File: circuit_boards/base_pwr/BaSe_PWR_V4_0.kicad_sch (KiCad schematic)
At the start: 105 parts, among them J1 12VDC In, J1 USB_C_Receptacle, J10 Conn_01x04_Socket, J11 MOTOR, J3 USB3_A, J3 USB_B_Micro, J4 Conn_01x07_Pin, J5 Conn_02x06_Odd_Even, J7 Conn_02x06_Odd_Even, J7 USB3_B_Micro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

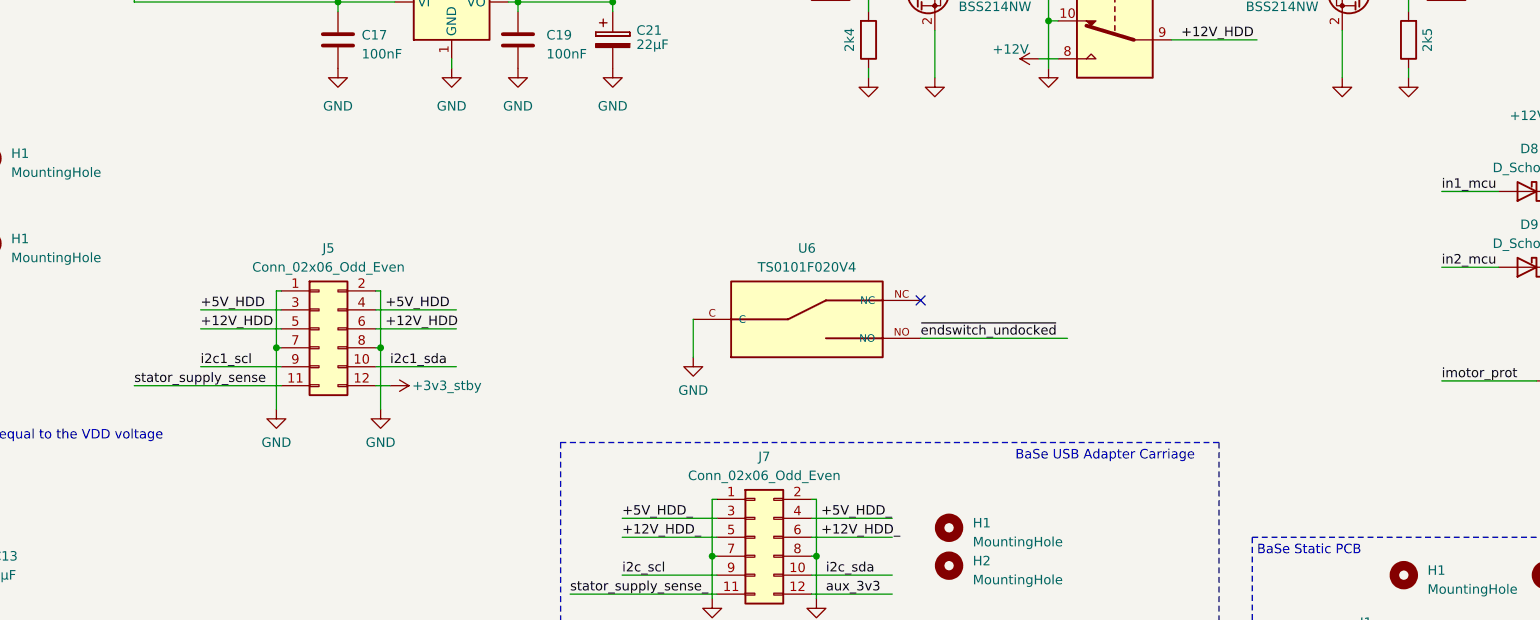
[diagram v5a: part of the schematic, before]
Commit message: BaSe PWR V4.0: rotate b2b connectors 180 degree for shorter pwr tracks
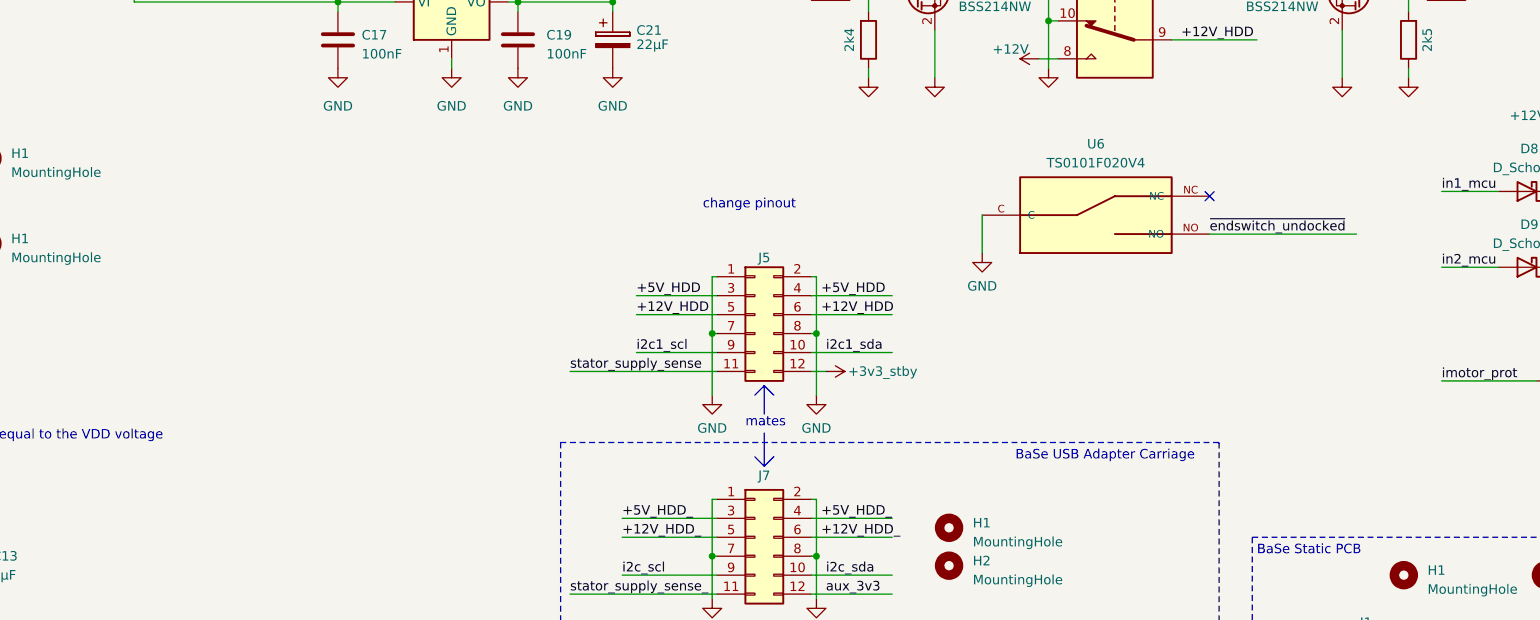
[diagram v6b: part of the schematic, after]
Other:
- note added: "change pinout"
- note added: "mates"
- moved on the sheet: J5, U6

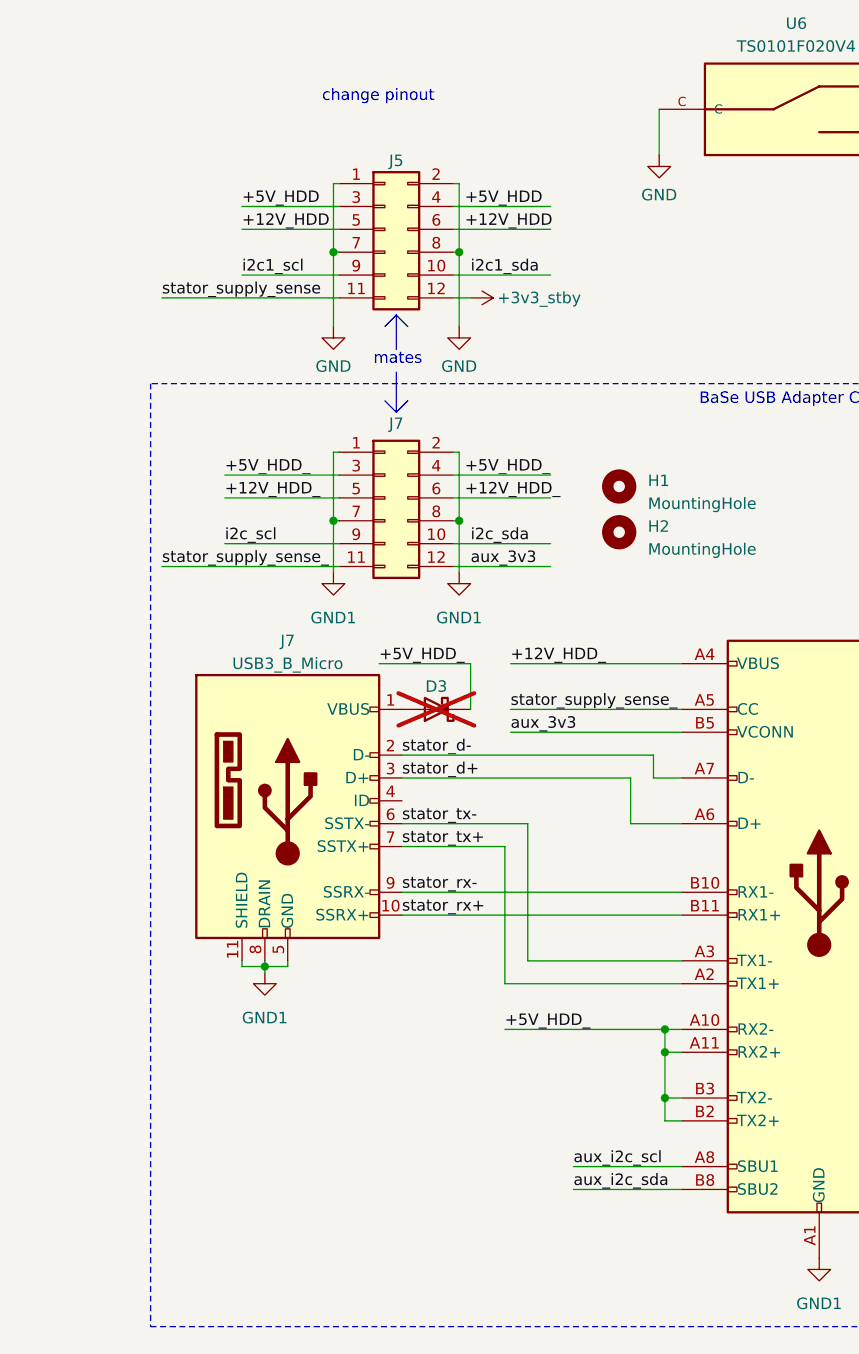
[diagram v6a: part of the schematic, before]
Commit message: Base PWR V4.0: optimize pinout for b2b connectors
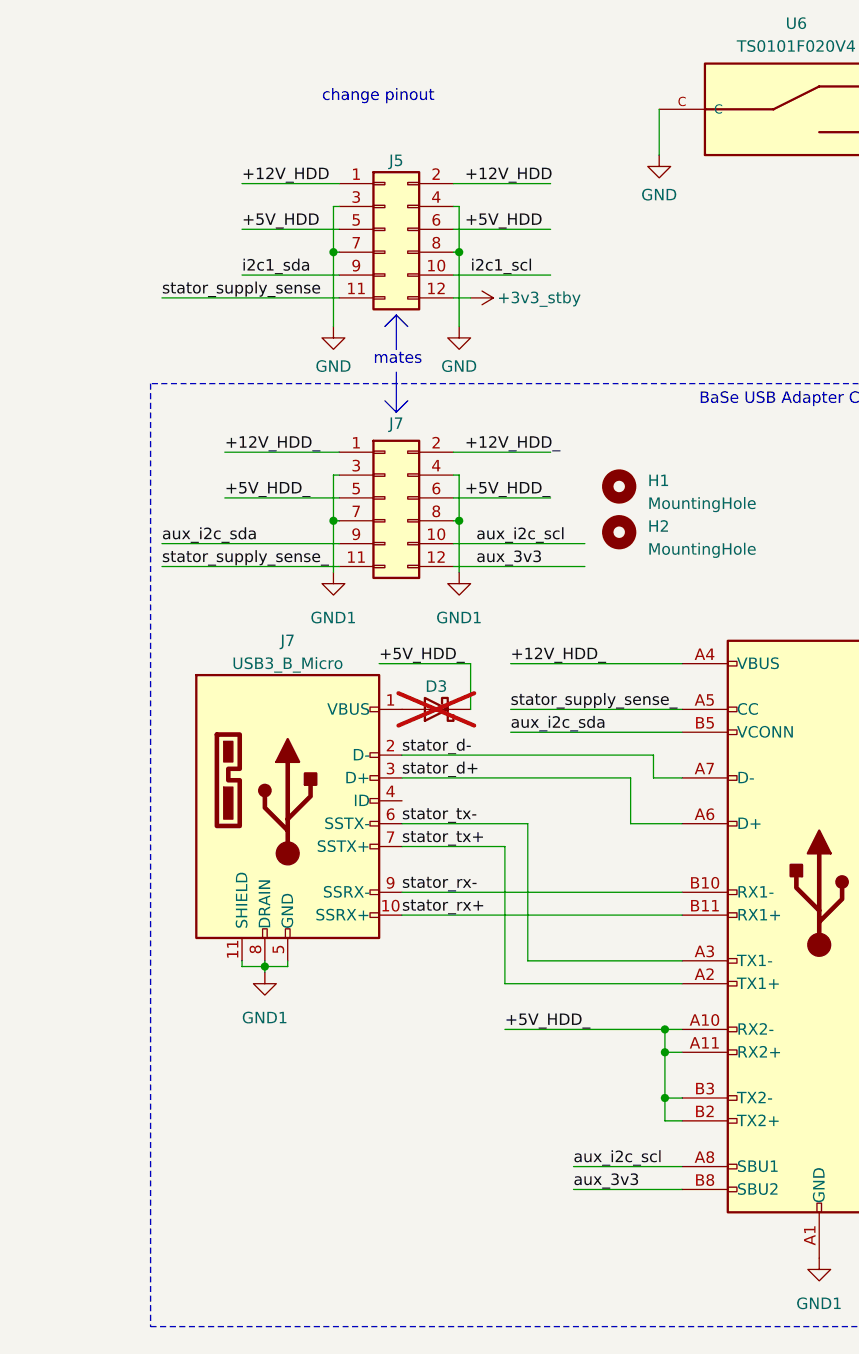
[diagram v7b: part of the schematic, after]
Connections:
- net i2c_scl is gone; now on net aux_i2c_sda: J7.9 (Pin_9)
- net i2c_sda is gone; now on net aux_i2c_scl: J7.10 (Pin_10)
- net +12V_HDD: now also J5.1 (Pin_1), J5.2 (Pin_2); no longer J5.5 (Pin_5), J5.6 (Pin_6)
- net +12V_HDD_: now also J7.1 (Pin_1), J7.2 (Pin_2); no longer J7.5 (Pin_5), J7.6 (Pin_6)
- net +5V_HDD: now also J5.5 (Pin_5), J5.6 (Pin_6); no longer J5.3 (Pin_3), J5.4 (Pin_4)
- net +5V_HDD_: now also J7.5 (Pin_5), J7.6 (Pin_6); no longer J7.3 (Pin_3), J7.4 (Pin_4)
- net GND: now also J5.3 (Pin_3), J5.4 (Pin_4); no longer J5.1 (Pin_1), J5.2 (Pin_2)
- net GND1: now also J7.3 (Pin_3), J7.4 (Pin_4); no longer J7.1 (Pin_1), J7.2 (Pin_2)
- net aux_3v3: now also P1.B8 (SBU2); no longer P1.B5 (VCONN)
- net aux_i2c_sda: now also P1.B5 (VCONN); no longer P1.B8 (SBU2)
- net i2c1_scl: now also J5.10 (Pin_10); no longer J5.9 (Pin_9)
- net i2c1_sda: now also J5.9 (Pin_9); no longer J5.10 (Pin_10)

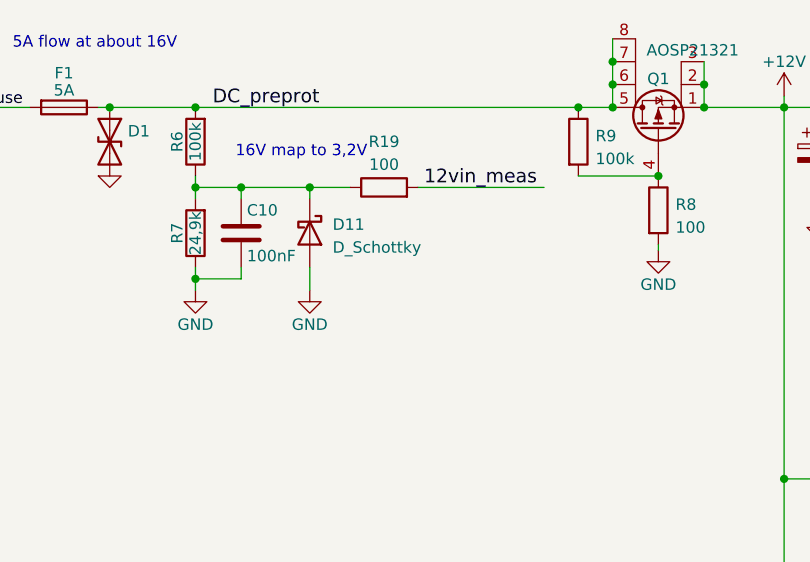
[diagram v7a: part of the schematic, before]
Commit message: BaSe PWR V4.0: resolve DRC errors
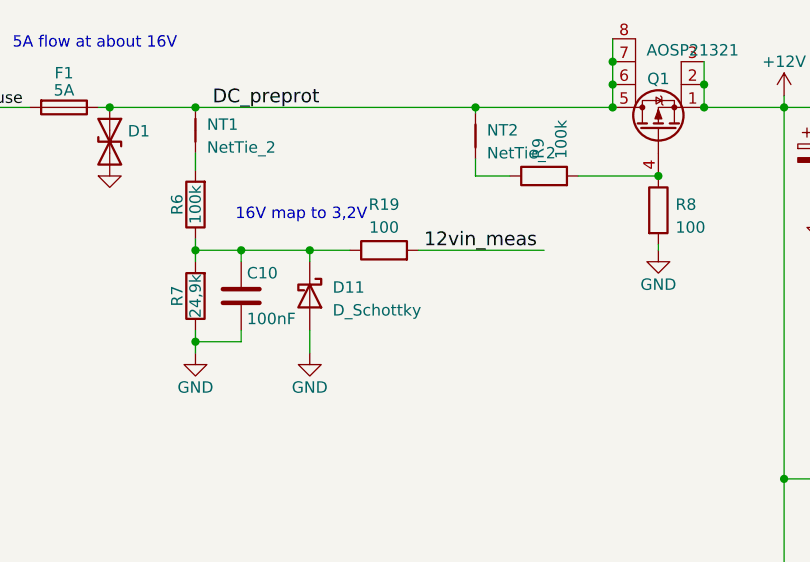
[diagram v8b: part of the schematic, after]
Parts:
- added NT1, NT2: NetTie_2, NetTie:NetTie-2_SMD_Pad0.5mm, symbol Device:NetTie_2
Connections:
- net DC_preprot: now also NT1.2, NT2.2; no longer R6.2, R9.1
- new net: NT1.1, R6.2
- new net: NT2.1, R9.1
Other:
- moved on the sheet: C10, D11, R19, R6, R7, R9
